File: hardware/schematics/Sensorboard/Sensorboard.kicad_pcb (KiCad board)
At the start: 2 copper layers, 138 x 76 mm, 79 parts, among them J1 Grauwasser, J3 BME680 #0 Innen, J4 RS485, J5 BME680 #1 Außen, J6 HX711 GasWaage, J7 LT452 Malibu, J8 Frischwasser, Q1 BSS138, Q2 BSS138, Q3 BSS138, Q4 AO3401A, Q5 2N7002, Q6 BSS138, Q7 BSS138, U1 ESP32-S3-DevKitC, U2 TSR2-2450, U3 LDL1117S33R, U4 SP3485CP, U5 PCF8523T, U6 BNO055, Y1 32.768

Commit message: feat(sensorboard): INA226, Web-Dashboard, Memory-Bank + Schematics-Update
Sensorboard:
- INA226 Strom-/Leistungsmessung integriert (k0i05/esp_ina226 v1.2.7)
- elec-Topic (5s) über RS485 und HTTP-API
- Web-Dashboard (SPIFFS, /api/*, mDNS Womo-Sensor.local)
- Memory-Bank angelegt (projectbrief, techContext, systemPatterns, productContext, activeContext, progress)
- Claude Code Settings hinzugefügt (.claude/)

Hardware:
- SensorBee + Sensorboard KiCad-Schematics aktualisiert
- Exportierte PDF/SVG-Fab-Ausgaben hinzugefügt
- Auto-Saved-File entfernt

Sonstiges:
- Root CLAUDE.md hinzugefügt
- Router-WebUI und Website aktualisiert
- Ducato-Bild-Assets (sdcard/images) hinzugefügt

Co-Authored-By: Claude Sonnet 4.6 <noreply@anthropic.com>
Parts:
- removed TP1: USB PWR, Connector_PinHeader_2.54mm:PinHeader_1x02_P2.54mm_Vertical
- added J2: Switch/Solder Jumper, Connector_PinHeader_2.54mm:PinHeader_1x02_P2.54mm_Vertical, F.Cu at (102.0, 85.7)
- added J9: USB Power, Connector_PinHeader_2.54mm:PinHeader_1x02_P2.54mm_Vertical, F.Cu at (191.5, 111.0)
- added R32: 10m, Resistor_SMD:R_2512_6332Metric_Pad1.40x3.35mm_HandSolder, F.Cu at (102.0, 75.5)
- added U7: INA226, Package_SO:VSSOP-10_3x3mm_P0.5mm, F.Cu at (110.0, 91.5)
- Q1, Q2, Q3, Q6, Q7: value BSS138 -> IRLML2244
- TP2: footprint TestPoint:TestPoint_THTPad_2.0x2.0mm_Drill1.0mm -> TestPoint:TestPoint_THTPad_3.0x3.0mm_Drill1.5mm
- moved C5 3.04 mm to (109.0, 85.5)
- moved R1 3.04 mm to (109.0, 71.3)
- moved R2 3.04 mm to (111.5, 71.5)
- moved R3 3.04 mm to (112.5, 85.5)
- moved U4 3.04 mm to (111.0, 79.0)
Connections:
- C1 pad 1: /WB -> Net-(D3-K)
- D3 pad 1: /WB -> Net-(D3-K)
- D4 pad 1: /WB -> Net-(D3-K)
- D5 pad 1: /WB -> Net-(D3-K)
- D6 pad 1: /WB -> Net-(D3-K)
- D7 pad 1: /WB -> Net-(D3-K)
- J1 pad 1: /WB -> Net-(D3-K)
- J8 pad 1: /WB -> Net-(D3-K)
- R19 pad 1: /WB -> Net-(D3-K)
- U2 pad 1: /WB -> Net-(D3-K)
- U3 pad 2: unconnected-(U3-VO-Pad2) -> +3.3V
- U3 pad 3: unconnected-(U3-VI-Pad3) -> /+5V
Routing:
- net /WB: track 217.5 -> 0.00 mm, vias 2 -> 0
- net Net-(D3-K): track 0.00 -> 199.9 mm, vias 0 -> 1
- net GND: track 753.4 -> 652.2 mm, vias 15 -> 14
- net /Multimedia: track 153.4 -> 120.8 mm, vias 2 -> 3
- net /SB: track 120.6 -> 89.9 mm, vias 3 -> 2
- net /Licht: track 109.9 -> 139.6 mm, vias 0 -> 2
- net Net-(U7-Vin+): track 0.00 -> 26.4 mm, vias 0 -> 2
- net Net-(U1-GPIO10/ADC1_CH9): track 72.7 -> 59.7 mm
- net /I2C SCL: track 111.9 -> 124.4 mm, vias 2 -> 4
- net Net-(U1-GPIO14/ADC2_CH3): track 101.0 -> 113.4 mm, vias 2 -> 1
- net /+5V: track 196.9 -> 207.8 mm, vias 3 -> 1
- net /Pumpe: track 126.7 -> 136.1 mm
- net Net-(U1-GPIO13/ADC2_CH2): track 71.9 -> 80.8 mm
- net +3.3V: track 158.2 -> 149.5 mm, vias 2 -> 7
- net Net-(J2-Pin_1): track 0.00 -> 7.17 mm
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
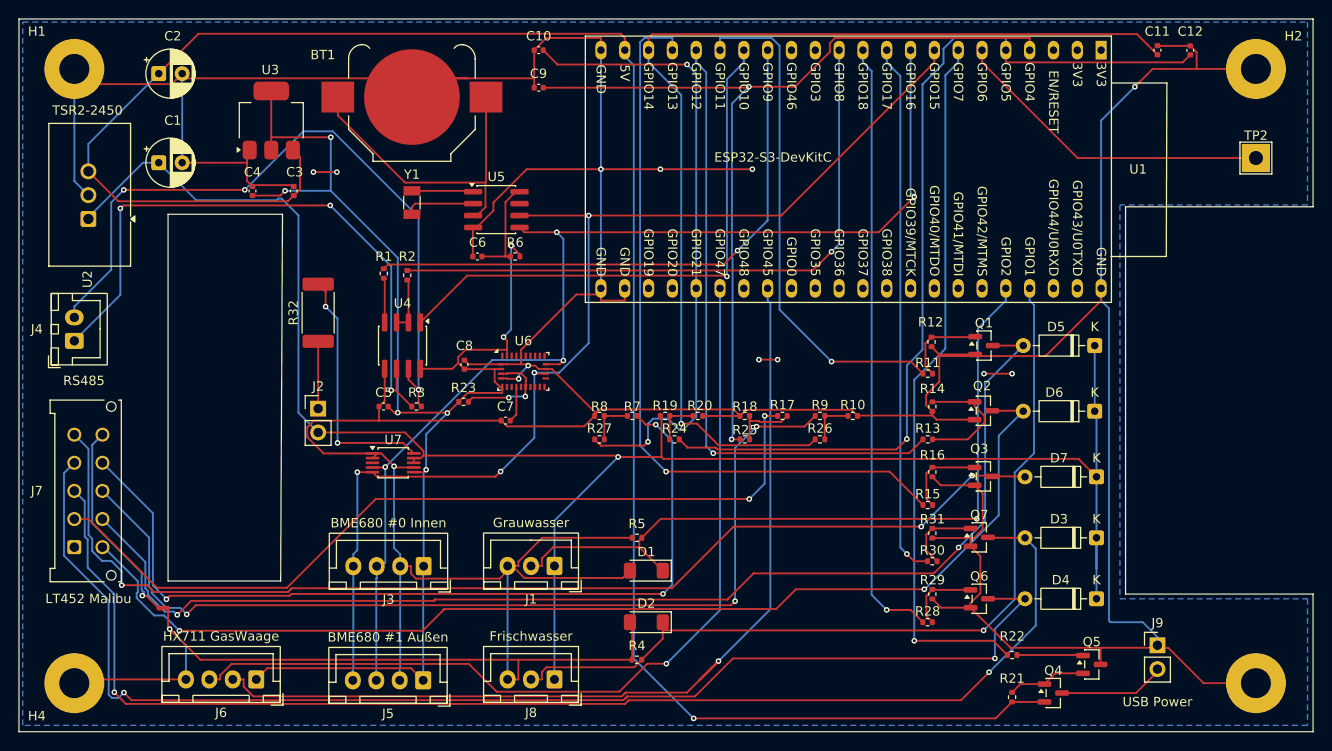
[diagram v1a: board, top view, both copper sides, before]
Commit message: hw(schematics): Sensorboard KiCad-Dateien aktualisiert
PCB, Schaltplan, Projektdatei und Fabrication-Optionen nach letzten
Überarbeitungen auf neuer Platine (INA226, Q5-Treiber, BNO055).

Co-Authored-By: Claude Sonnet 4.6 <noreply@anthropic.com>
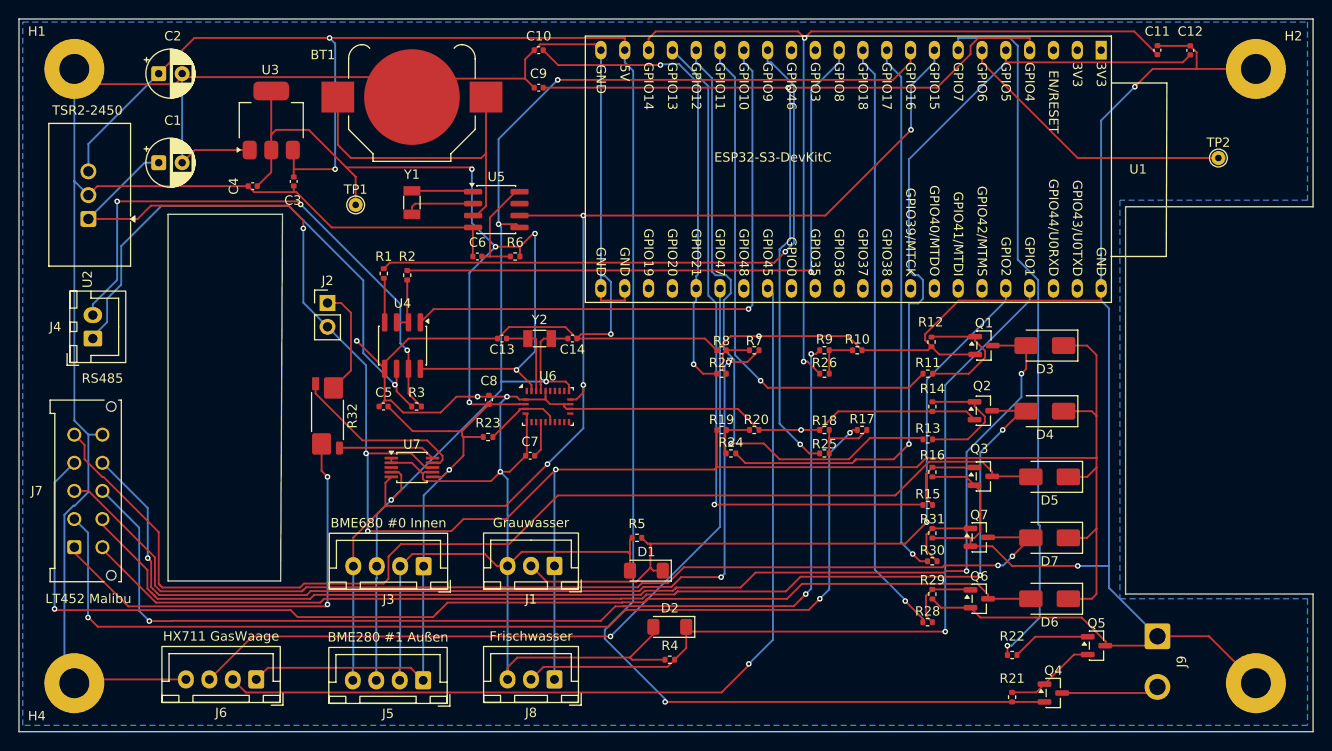
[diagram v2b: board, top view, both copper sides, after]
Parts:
- removed NT1: Masse <-> GND, NetTie:NetTie-2_SMD_Pad0.5mm
- added C13: 12pF, Capacitor_SMD:C_0402_1005Metric, F.Cu at (121.6, 78.2)
- added C14: 12pF, Capacitor_SMD:C_0402_1005Metric, F.Cu at (129.1, 78.2)
- added TP1: Power 3.3 Test, TestPoint:TestPoint_THTPad_D1.5mm_Drill0.7mm, F.Cu at (106.0, 64.0)
- added Y2: 32.768, Crystal:Crystal_SMD_3215-2Pin_3.2x1.5mm, F.Cu at (125.6, 78.2)
- D3, D4, D5, D6, D7: value 1N4148 -> SS14; footprint Diode_THT:D_DO-35_SOD27_P7.62mm_Horizontal -> Diode_SMD:D_SMA
- J5: value BME680 #1 Außen -> BME280 #1 Außen
- J9: footprint Connector_PinHeader_2.54mm:PinHeader_1x02_P2.54mm_Vertical -> Connector_Wire:SolderWire-1sqmm_1x02_P5.4mm_D1.4mm_OD2.7mm
- R32: footprint Resistor_SMD:R_2512_6332Metric_Pad1.40x3.35mm_HandSolder -> Resistor_SMD:R_Shunt_Vishay_WSK2512_6332Metric_T1.19mm
- TP2: footprint TestPoint:TestPoint_THTPad_3.0x3.0mm_Drill1.5mm -> TestPoint:TestPoint_THTPad_D1.5mm_Drill0.7mm
- moved D3 21.2 mm to (179.5, 79.0)
- moved D4 20.7 mm to (179.5, 86.0)
- moved D6 20.6 mm to (180.0, 106.0)
- moved D5 14.8 mm to (180.0, 93.0)
- moved R27 14.8 mm to (145.0, 82.0)
- moved R7 14.8 mm to (148.5, 79.5)
- moved R8 14.8 mm to (145.0, 79.5)
- moved J2 11.3 mm to (103.0, 74.5)
- moved R32 11.0 mm to (103.0, 86.5), turned to -90 degrees
- moved R17 8.62 mm to (160.0, 88.0)
- moved R18 8.62 mm to (156.0, 88.0)
- moved R25 8.62 mm to (156.0, 90.5)
- moved D7 8.20 mm to (180.0, 99.5)
- moved R10 7.02 mm to (159.5, 79.5)
- moved R26 7.02 mm to (156.0, 82.0)
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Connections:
- net /+5V renamed +5V
- C1 pad 1: Net-(D3-K) -> +12V
- D3 pad 1: Net-(D3-K) -> +12V
- D3 pad 2: /Licht -> /12V - EIN
- D4 pad 1: Net-(D3-K) -> +12V
- D4 pad 2: /Pumpe -> /12V - AUS
- D5 pad 1: Net-(D3-K) -> +12V
- D5 pad 2: /12V - EIN -> /Multimedia
- D6 pad 1: Net-(D3-K) -> +12V
- D6 pad 2: /12V - AUS -> /Pumpe
- D7 pad 1: Net-(D3-K) -> +12V
- D7 pad 2: /Multimedia -> /Licht
- J1 pad 1: Net-(D3-K) -> +12V
- J2 pad 2: Net-(D3-K) -> +12V
- J7 pad 10: /Masse -> GND
- J8 pad 1: Net-(D3-K) -> +12V
- R19 pad 1: Net-(D3-K) -> +12V
- R32 pad 2: Net-(U7-Vin+) -> Net-(U7-Vin-)
- U2 pad 1: Net-(D3-K) -> +12V
- U6 pad 17: /I2C SCL -> GND
- U6 pad 19: /I2C SDA -> /I2C SCL
- U6 pad 20: unconnected-(U6-COM0-Pad20) -> /I2C SDA
- U6 pad 26: unconnected-(U6-XOUT32-Pad26) -> Net-(U6-XOUT32)
- U6 pad 27: unconnected-(U6-XIN32-Pad27) -> Net-(U6-XIN32)
- U6 pad 6: +3.3V -> GND
- U7 pad 8: Net-(D3-K) -> +12V
- U7 pad 9: Net-(D3-K) -> Net-(U7-Vin-)
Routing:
- net +12V: track 0.00 -> 228.4 mm, vias 0 -> 4
- net Net-(D3-K): track 199.9 -> 0.00 mm, vias 1 -> 0
- net /WB: track 0.00 -> 47.4 mm, vias 0 -> 2
- net GND: track 652.2 -> 695.5 mm, vias 14 -> 9
- net /Licht: track 139.6 -> 115.4 mm
- net /Masse: track 22.3 -> 0.00 mm, vias 1 -> 0
- net +3.3V: track 149.5 -> 170.6 mm, vias 7 -> 6
- net /SB: track 89.9 -> 110.7 mm, vias 2 -> 3
- net Net-(U1-GPIO14/ADC2_CH3): track 113.4 -> 94.2 mm, vias 1 -> 2
- net Net-(U7-Vin-): track 0.00 -> 19.0 mm
- net Net-(U1-GPIO21): track 68.4 -> 51.1 mm
- net Net-(J4-Pin_2): track 76.6 -> 59.8 mm
- net Net-(U7-Vin+): track 26.4 -> 10.4 mm, vias 2 -> 0
- net /Pumpe: track 136.1 -> 123.2 mm, vias 2 -> 1
- net /Netz: track 93.2 -> 104.4 mm
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
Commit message: chore: OpenWiki, Sensorboard-/ruuvitag_gas-Schaltplaene, Log-Level und Doku nachgezogen
- OpenWiki-Index (openwiki/, AGENTS.md) und Verweis in CLAUDE.md
- Sensorboard-Schaltplan/PCB und ruuvitag_gas-Schaltplan aktualisiert
- LDL1117S33R-Bauteilbibliothek, Material-Icon-Font 16 px
- display_config.h: Log-Level Main/Theme auf WARN, Screenshot-Block aufgeraeumt
- gasbee_nrf/README: HX711-Modul und AVDD-Spannungsteiler beschrieben
- ruuvitag_hw (Fremd-Repo) in .gitignore

Co-Authored-By: Claude Opus 5.5 <noreply@anthropic.com>
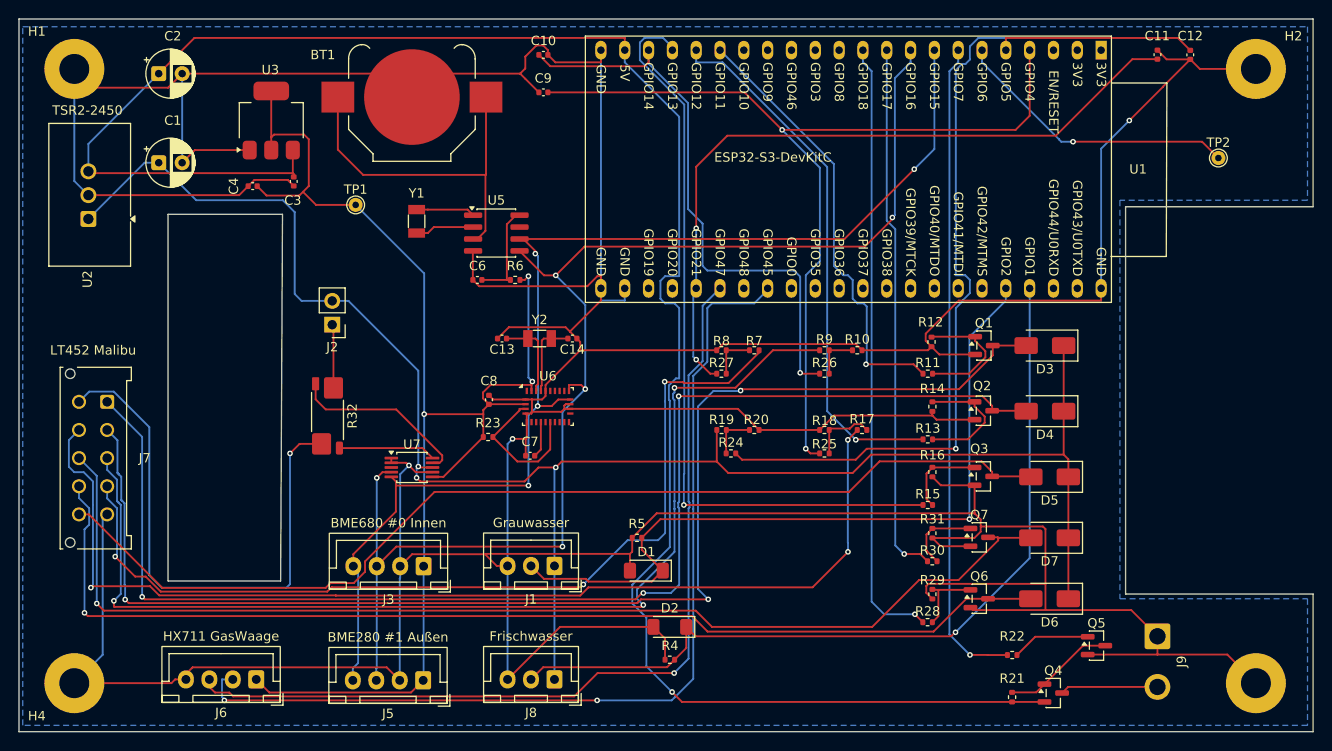
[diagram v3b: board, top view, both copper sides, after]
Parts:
- removed C5: 100nF, Capacitor_SMD:C_0402_1005Metric
- removed J4: RS485, Connector_JST:JST_XH_B2B-XH-A_1x02_P2.50mm_Vertical
- removed R1, R2: 100, Resistor_SMD:R_0402_1005Metric
- removed R3: 120, Resistor_SMD:R_0402_1005Metric
- removed U4: SP3485CP, Package_SO:SOIC-8_3.9x4.9mm_P1.27mm
- moved J7 15.9 mm to (79.5, 85.0), turned to -90 degrees
- moved C6 2.50 mm to (119.0, 72.0)
- moved R6 2.50 mm to (123.0, 72.0)
- moved U5 2.50 mm to (121.0, 67.0)
- moved J2 2.37 mm to (103.5, 76.8), turned to 180 degrees
- moved Y1 2.06 mm to (112.5, 65.8)
- moved C10 0.71 mm to (126.0, 48.0)
- moved C9 0.71 mm to (126.0, 52.0)
- moved C11 0.48 mm to (191.5, 48.0)
- moved C12 0.48 mm to (195.0, 48.0)
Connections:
- C10 pad 1: Net-(U1-GPIO21) -> GND
- C10 pad 2: GND -> Net-(U1-GPIO14/ADC2_CH3)
- C11 pad 2: Net-(U1-GPIO14/ADC2_CH3) -> Net-(U1-GPIO21)
- C12 pad 1: Net-(U1-GPIO5/ADC1_CH4) -> GND
- C12 pad 2: GND -> Net-(U1-GPIO5/ADC1_CH4)
- J7 pad 1: /WB -> /12V - AUS
- J7 pad 10: GND -> /Multimedia
- J7 pad 2: /SB -> /12V - EIN
- J7 pad 3: /Licht -> /12V - Kontrolle
- J7 pad 4: /Pumpe -> /Netz
- J7 pad 5: /Multimedia -> GND
- J7 pad 6: /12V - AUS -> /WB
- J7 pad 7: /12V - EIN -> /SB
- J7 pad 8: /12V - Kontrolle -> /Licht
- J7 pad 9: /Netz -> /Pumpe
- Q5 pad 2: Net-(Q4-G) -> GND
- Q5 pad 3: GND -> Net-(Q4-G)
- U1 pad 12: Net-(U1-GPIO8/ADC1_CH7) -> unconnected-(U1-GPIO8/ADC1_CH7-Pad12)
- U1 pad 15: Net-(U1-GPIO9/ADC1_CH8) -> unconnected-(U1-GPIO9/ADC1_CH8-Pad15)
- U1 pad 16: Net-(U1-GPIO10/ADC1_CH9) -> unconnected-(U1-GPIO10/ADC1_CH9-Pad16)
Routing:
- net Net-(U1-GPIO8/ADC1_CH7): track 68.1 -> 0.00 mm, vias 1 -> 0
- net Net-(U1-GPIO9/ADC1_CH8): track 66.8 -> 0.00 mm, vias 1 -> 0
- net Net-(U1-GPIO10/ADC1_CH9): track 63.7 -> 0.00 mm, vias 1 -> 0
- net Net-(J4-Pin_2): track 59.8 -> 0.00 mm, vias 3 -> 0
- net Net-(J4-Pin_1): track 59.4 -> 0.00 mm, vias 1 -> 0
- net +12V: track 228.4 -> 190.6 mm, vias 4 -> 3
- net GND: track 695.5 -> 658.6 mm, vias 9 -> 3
- net Net-(U1-GPIO14/ADC2_CH3): track 94.2 -> 62.3 mm, vias 2 -> 1
- net +3.3V: track 170.6 -> 142.5 mm, vias 6 -> 3
- net Net-(U1-GPIO21): track 51.1 -> 77.6 mm
- net /12V - AUS: track 121.2 -> 138.6 mm, vias 2 -> 3
- net /I2C SDA: track 126.7 -> 140.0 mm, vias 4 -> 5
- net /12V - EIN: track 129.3 -> 141.1 mm, vias 2 -> 3
- net /WB: track 47.4 -> 58.8 mm, vias 2 -> 1
- net Net-(U1-GPIO12/ADC2_CH1): track 67.2 -> 57.4 mm
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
